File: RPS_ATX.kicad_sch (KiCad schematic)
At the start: 35 parts, among them J1 494_ON, J10 MCU_FAN, J11 PW_IN, J13 FAN_OUT, J5 PS_OUT-, J6 PS_OUT+, J7 RPS_OUT-, J8 MEAS, J9 RPS_OUT+, Q3 AO3400A, U2 Mini360, U4 TL431DBZ, U5 LM358, U6 INA226, U7 LM7805_TO220

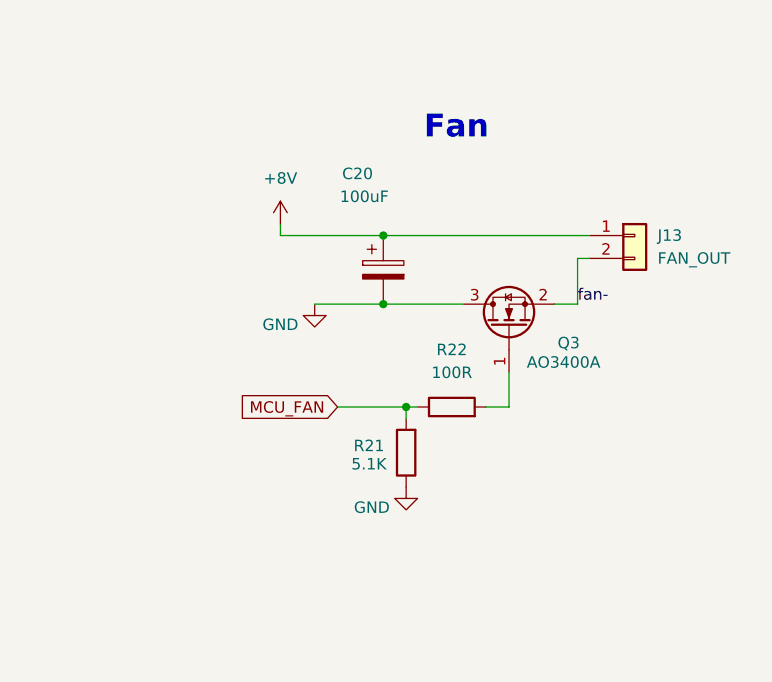
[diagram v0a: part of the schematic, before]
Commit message: rectified wrong fan transistor connection
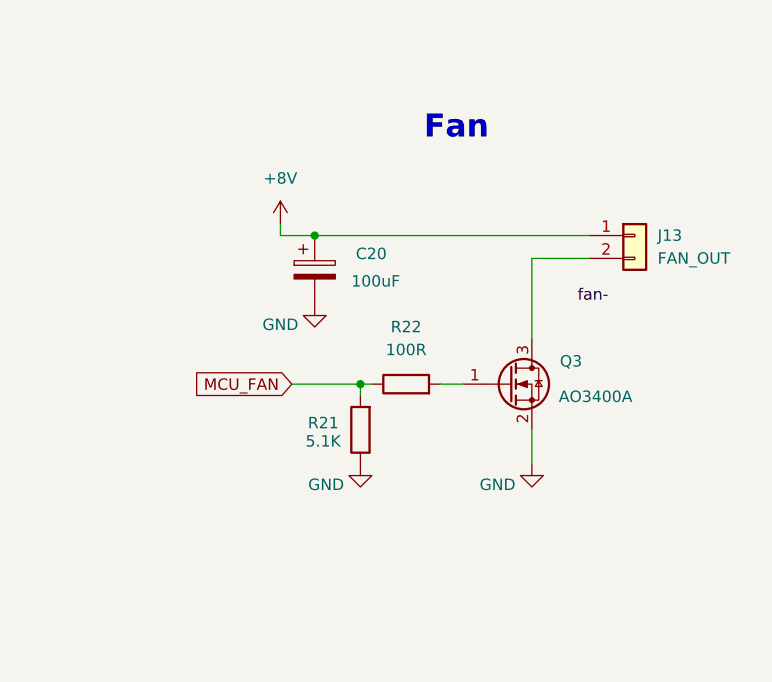
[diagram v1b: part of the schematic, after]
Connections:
- net GND: now also Q3.2 (S); no longer Q3.3 (D)
- net fan-: no longer J13.2 (Pin_2), Q3.2 (S)
- new net: J13.2 (Pin_2), Q3.3 (D)
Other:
- moved on the sheet: C20, Q3, R21, R22
